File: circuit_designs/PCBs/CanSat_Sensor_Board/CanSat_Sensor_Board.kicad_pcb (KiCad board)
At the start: 4 copper layers, 100 x 100 mm, 32 parts

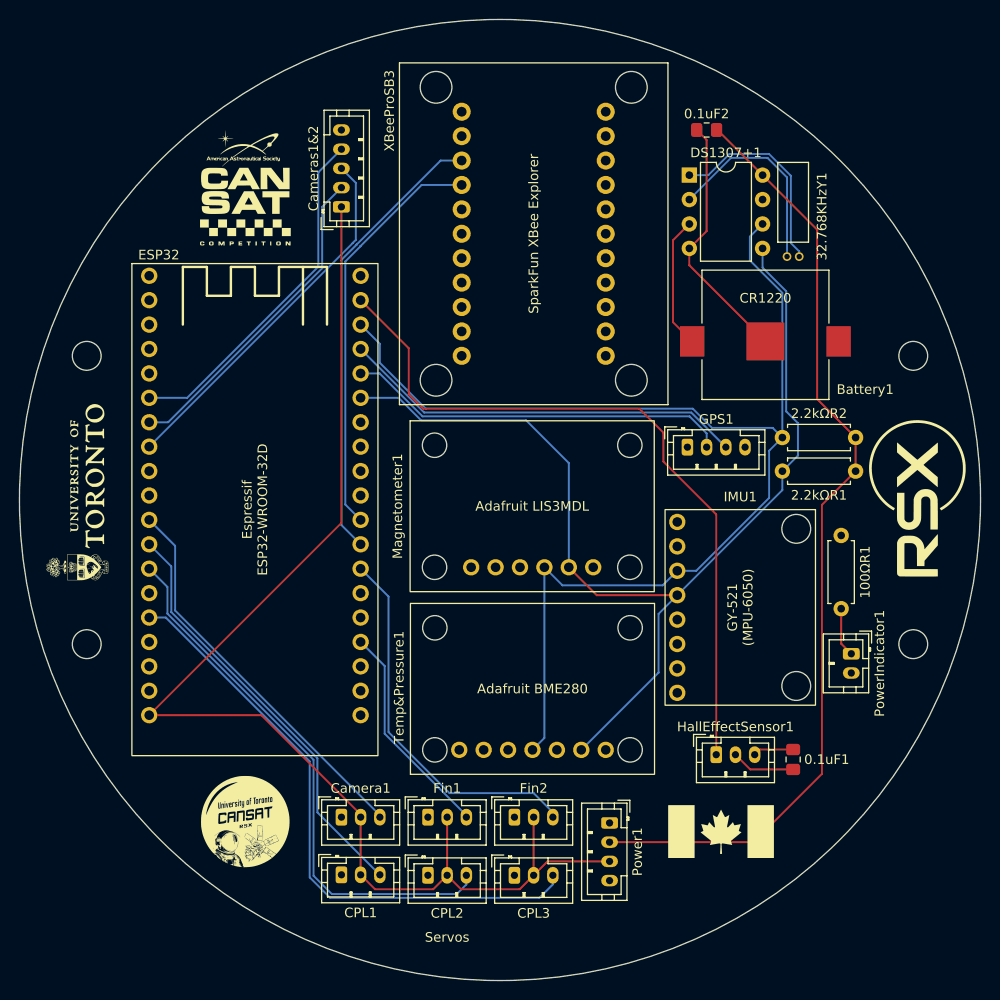
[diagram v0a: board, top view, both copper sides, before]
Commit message: Updating camera and sensor PCBs
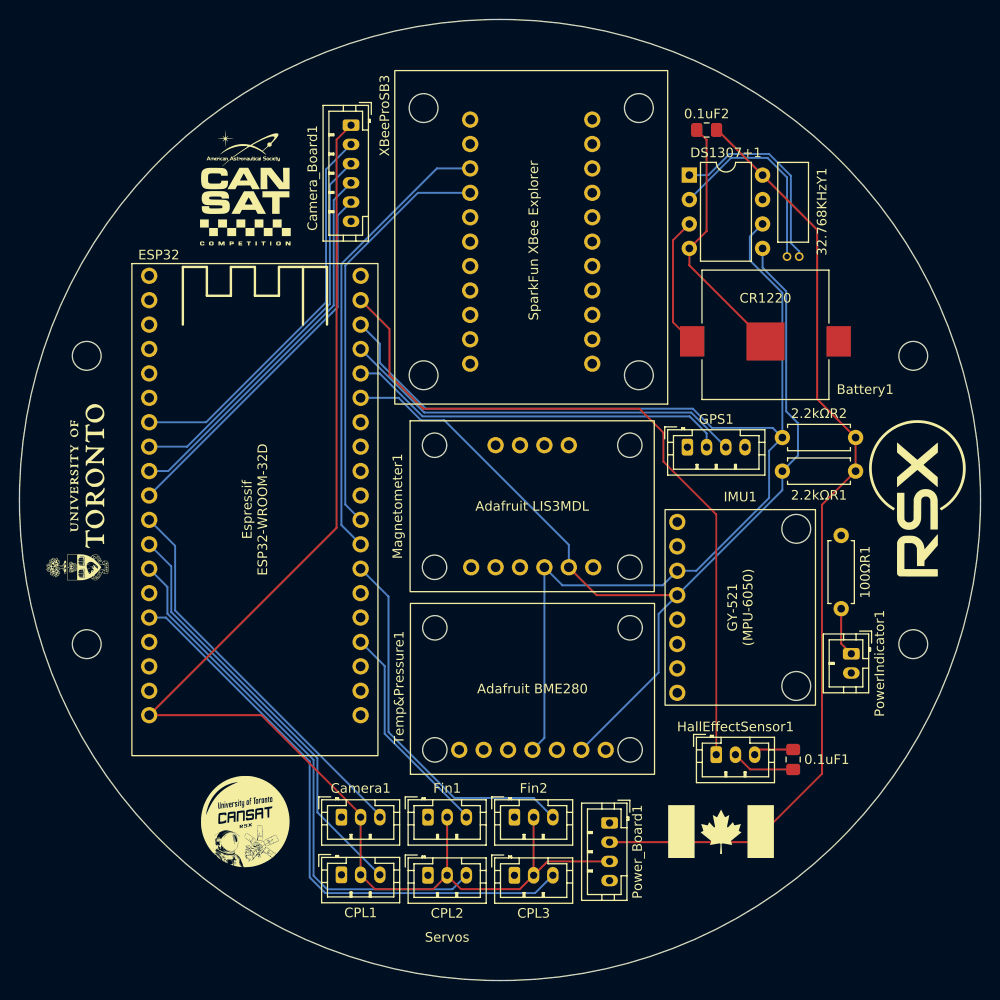
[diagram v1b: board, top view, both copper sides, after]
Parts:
- removed Cameras1&2: Conn_01x05_Pin, Connector_JST:JST_PH_B5B-PH-K_1x05_P2.00mm_Vertical
- added Camera_Board1: Conn_01x06_Pin, Connector_JST:JST_PH_B6B-PH-K_1x06_P2.00mm_Vertical, F.Cu at (134.5, 61.0)
- XBeeProSB3: footprint WRL-11812:MODULE_WRL-11812 -> Custom_Footprints:SparkFun_XBee_Explorer_Regulated
- moved XBeeProSB3 22.5 mm to (167.4, 90.0)
- renumbered Power1 to Power_Board1
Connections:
- ESP32 pad J2-10: unconnected-(ESP32-IO26-PadJ2-10) -> Net-(Camera_Board1-Pin_5)
- ESP32 pad J2-6: Net-(Cameras1&2-Pin_4) -> unconnected-(ESP32-IO35-PadJ2-6)
- ESP32 pad J2-9: unconnected-(ESP32-IO25-PadJ2-9) -> Net-(Camera_Board1-Pin_4)
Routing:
- net Net-(Camera_Board1-Pin_4): track 0.00 -> 39.8 mm
- net Net-(Camera_Board1-Pin_5): track 0.00 -> 39.2 mm
- net Net-(Cameras1&2-Pin_4): track 36.5 -> 0.00 mm
- net +7.4V: track 134.6 -> 143.5 mm
- net Net-(Camera_Board1-Pin_2): track 34.4 -> 41.1 mm
- net Net-(DS1307+1-SDA): track 111.1 -> 106.1 mm
- net Net-(Camera_Board1-Pin_3): track 38.5 -> 40.5 mm
- net Net-(CPL3-Pin_3): track 62.7 -> 61.7 mm
- net Net-(CPL2-Pin_3): track 57.1 -> 56.1 mm
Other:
- board text added: "Data1"
- board text added: "Data2"
- board text added: "Signal1"
- board text added: "Signal2"
- board text removed: "Cam1"
- board text removed: "Cam2"

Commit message: Updating new KiCad files
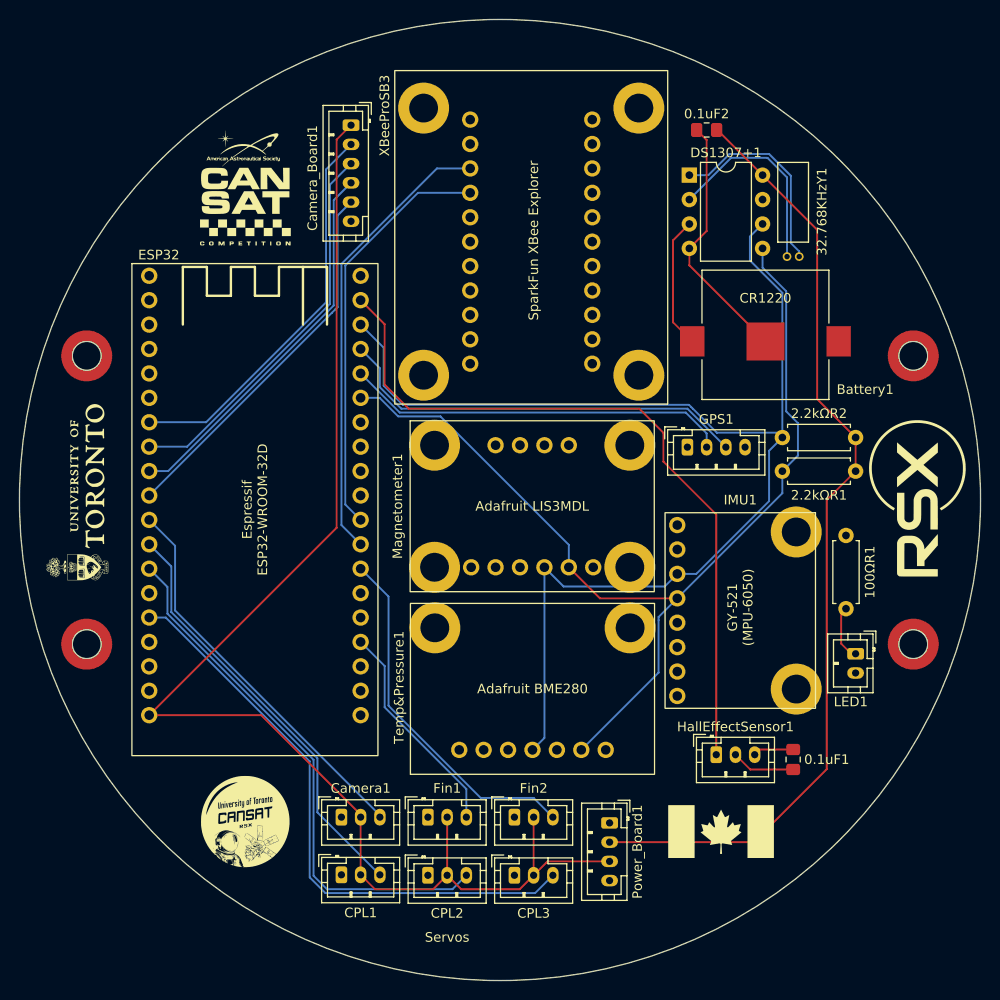
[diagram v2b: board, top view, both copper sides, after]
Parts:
- added REF**: WA-SMSI_9774030243, DigiKey:WA-SMSI_9774030243, F.Cu at (107.0, 85.0)
- added REF**: WA-SMSI_9774030243, DigiKey:WA-SMSI_9774030243, F.Cu at (193.0, 85.0)
- added REF**: WA-SMSI_9774030243, DigiKey:WA-SMSI_9774030243, F.Cu at (107.0, 115.0)
- added REF**: WA-SMSI_9774030243, DigiKey:WA-SMSI_9774030243, F.Cu at (193.0, 115.0)
- moved 100ΩR1 0.50 mm to (186.0, 111.3)
- moved LED1 0.45 mm to (187.0, 116.0)
- moved IMU1 0.33 mm to (182.8, 101.3)
- renumbered PowerIndicator1 to LED1
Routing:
- net Net-(ESP32-IO4): track 39.0 -> 37.4 mm
- net Net-(DS1307+1-SCL): track 128.9 -> 130.4 mm
- net Net-(ESP32-TXD0): track 42.2 -> 43.4 mm
- net Net-(ESP32-IO23): track 75.8 -> 76.7 mm
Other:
- outline, holes or cut-outs redrawn

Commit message: Final review submission of all CanSat PCB boards and corresponding custom KiCad 3D models, footprints, and symbols
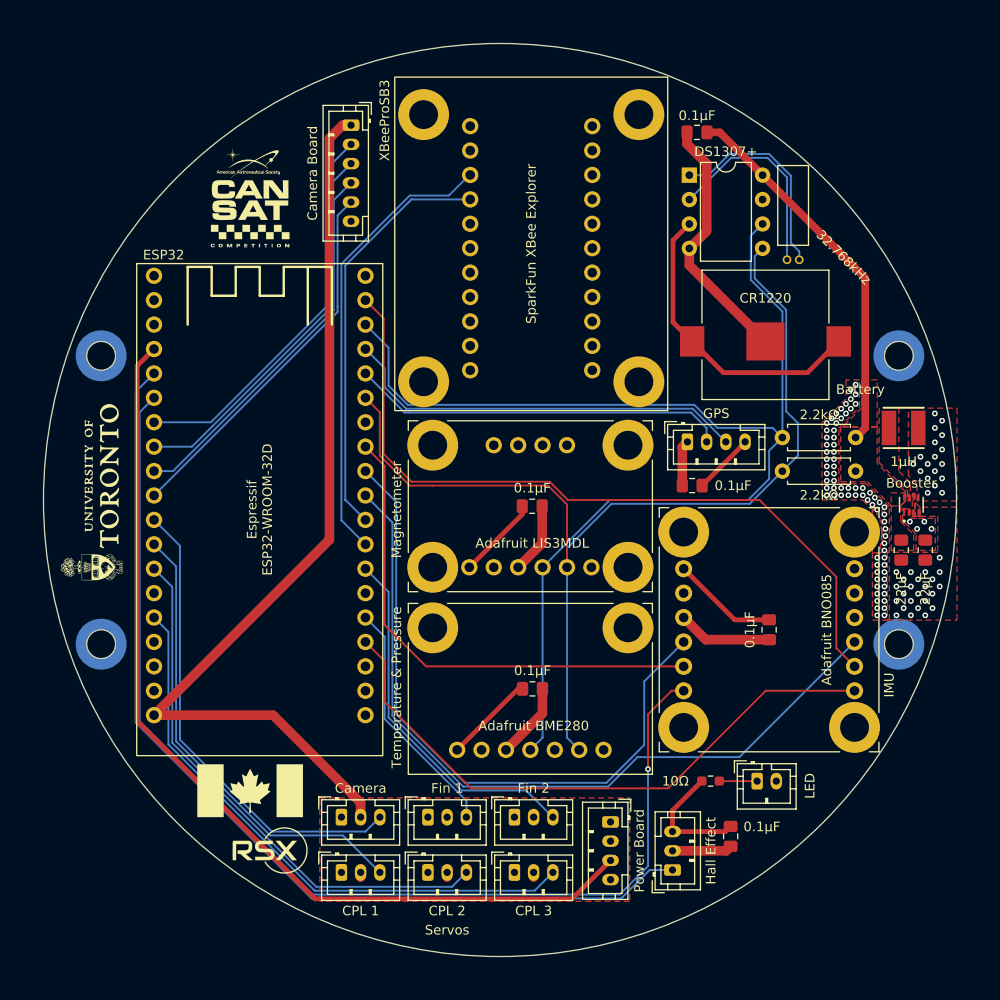
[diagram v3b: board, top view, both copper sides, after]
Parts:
- removed the G*** at (123.5, 67.5)
- removed the G*** at (193.5, 100.0)
- removed IMU1: GY-521_(MPU-6050), Custom_Footprints:GY-521_(MPU-6050)
- added Adafruit_BNO085_U5: IMU, Custom_Footprints:Adafruit_BNO085, F.Cu at (189.4, 100.8)
- added C2: 0.1μF, Capacitor_SMD:C_0805_2012Metric_Pad1.18x1.45mm_HandSolder, F.Cu at (153.4, 119.7)
- added C3: 0.1μF, Capacitor_SMD:C_0805_2012Metric_Pad1.18x1.45mm_HandSolder, F.Cu at (170.0, 98.5)
- added C4: 0.1μF, Capacitor_SMD:C_0805_2012Metric_Pad1.18x1.45mm_HandSolder, F.Cu at (153.3, 100.7)
- added C5: 0.1μF, Capacitor_SMD:C_0805_2012Metric_Pad1.18x1.45mm_HandSolder, F.Cu at (178.0, 113.5)
- added C7: 22μF, Capacitor_SMD:C_0805_2012Metric_Pad1.18x1.45mm_HandSolder, F.Cu at (194.2, 105.2)
- added C8: 22μF, Capacitor_SMD:C_0805_2012Metric_Pad1.18x1.45mm_HandSolder, F.Cu at (191.8, 105.2)
- added G***: LOGO, Graphics:cansat_logo_2, F.Cu at (124.0, 68.5)
- added G***: LOGO, Graphics:rsx_logo_3, F.Cu at (126.0, 136.5)
- added G***: LOGO, Graphics:rsx_logo_2, B.Cu at (153.0, 115.0)
- added TPS610333DRLR_U8: Booster, DigiKey:SOT-5X3-8_DRL_TEX, F.Cu at (192.8, 100.5)
- added WE-LQS_4025_L1: 1μH, DigiKey:WE-LQS_4025, F.Cu at (192.0, 92.5)
- 2894TR_U7: renamed from Battery1; value 2894TR -> Battery
- Adafruit_BME280_STEMMA_QT_U3: renamed from Temp&Pressure1; value Adafruit_BME280_STEMMA_QT -> Temperature & Pressure
- Adafruit_LIS3MDL_U4: renamed from Magnetometer1; value Adafruit_LIS3MDL -> Magnetometer
- C1: renamed from 0.1uF1; value C1 -> 0.1μF
- C6: renamed from 0.1uF2; value C2 -> 0.1μF
- ESP32-DEVKIT-32_U1: renamed from ESP32; value ESP32-DEVKITC-32D -> ESP32
- G***, REF** (x4): moved to B.Cu
- J1: renamed from Power_Board1; value Conn_01x04_Pin -> Power Board
- J10: renamed from CPL2; value Conn_01x03_Pin -> CPL 2
- J11: renamed from CPL3; value Conn_01x03_Pin -> CPL 3
- J2: renamed from Camera_Board1; value Conn_01x06_Pin -> Camera Board
- J3: renamed from HallEffectSensor1; value Conn_01x03_Pin -> Hall Effect
- J4: renamed from GPS1; value Conn_01x04_Pin -> GPS
- J5: renamed from LED1; value Conn_01x02_Pin -> LED
- J6: renamed from Fin1; value Conn_01x03_Pin -> Fin 1
- J7: renamed from Fin2; value Conn_01x03_Pin -> Fin 2
- J8: renamed from Camera1; value Conn_01x03_Pin -> Camera
- J9: renamed from CPL1; value Conn_01x03_Pin -> CPL 1
- R1: renamed from 100ΩR1; value R1 -> 10Ω; footprint Resistor_THT:R_Axial_DIN0207_L6.3mm_D2.5mm_P7.62mm_Horizontal -> Resistor_SMD:R_0603_1608Metric_Pad0.98x0.95mm_HandSolder
- R2: renamed from 2.2kΩR1; value R2 -> 2.2kΩ
- R3: renamed from 2.2kΩR2; value R3 -> 2.2kΩ
- SparkFunXBeeExplorer_U2: renamed from XBeeProSB3; value SparkFunXBeeExplorer1 -> XBeeProSB3
- Y1: renamed from 32.768KHzY1; value AB38T-32.768KHZ -> 32.768kHz
- moved G*** 62.0 mm to (178.0, 104.0), turned to 180 degrees
- moved G*** 49.2 mm to (124.0, 130.2)
- moved R1 22.8 mm to (171.9, 129.2), turned to 180 degrees
- moved J5 16.8 mm to (176.8, 129.2), turned to 0 degrees
- moved J3 12.8 mm to (167.9, 138.5), turned to 90 degrees
- moved C1 10.3 mm to (174.0, 135.0), turned to 90 degrees
- moved G*** 1.50 mm to (108.5, 97.5)
- moved G*** 1.50 mm to (107.5, 107.0)
- moved REF** 1.50 mm to (108.5, 85.0), turned to 180 degrees
- moved REF** 1.50 mm to (191.5, 85.0), turned to 180 degrees
- moved REF** 1.50 mm to (108.5, 115.0), turned to 180 degrees
- moved REF** 1.50 mm to (191.5, 115.0), turned to 180 degrees
- moved C6 1.03 mm to (170.5, 61.8)
- moved SparkFunXBeeExplorer_U2 0.68 mm to (167.4, 90.7)
- moved J4 0.55 mm to (169.5, 94.0)
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- renumbered DS1307+1 to DS1307+_U6
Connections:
- 2894TR_U7 pad P1: unconnected-(Battery1-PadP1) -> Net-(DS1307+_U6-VBAT)
- 2894TR_U7 pad P2: Net-(DS1307+1-VBAT) -> Net-(DS1307+_U6-VBAT)
- Adafruit_BME280_STEMMA_QT_U3 pad 1: +3.3V -> /3.3V
- Adafruit_LIS3MDL_U4 pad 1: +3.3V -> /3.3V
- C1 pad 1: +3.3V -> GND
- C1 pad 2: GND -> /3.3V
- C6 pad 2: +5V -> /5V
- DS1307+_U6 pad 3: Net-(DS1307+1-VBAT) -> Net-(DS1307+_U6-VBAT)
- DS1307+_U6 pad 8: +5V -> /5V
- ESP32-DEVKIT-32_U1 pad J2-19: +7.4V -> /7.4V
- ESP32-DEVKIT-32_U1 pad J2-4: unconnected-(ESP32-SENSOR_VN-PadJ2-4) -> /ADC
- ESP32-DEVKIT-32_U1 pad J2-5: unconnected-(ESP32-IO34-PadJ2-5) -> Net-(ESP32-DEVKIT-32_U1-IO34)
- ESP32-DEVKIT-32_U1 pad J2-6: unconnected-(ESP32-IO35-PadJ2-6) -> Net-(Adafruit_BNO085_U5-~{INT})
- ESP32-DEVKIT-32_U1 pad J3-10: unconnected-(ESP32-IO5-PadJ3-10) -> Net-(Adafruit_BNO085_U5-~{RST})
- ESP32-DEVKIT-32_U1 pad J3-15: unconnected-(ESP32-IO2-PadJ3-15) -> Net-(ESP32-DEVKIT-32_U1-IO2)
- ESP32-DEVKIT-32_U1 pad J3-16: Net-(ESP32-IO15) -> Net-(Adafruit_BNO085_U5-CS)
- ESP32-DEVKIT-32_U1 pad J3-2: Net-(ESP32-IO23) -> Net-(Adafruit_BNO085_U5-DI)
- ESP32-DEVKIT-32_U1 pad J3-8: unconnected-(ESP32-IO19-PadJ3-8) -> Net-(Adafruit_BNO085_U5-SDA)
- ESP32-DEVKIT-32_U1 pad J3-9: unconnected-(ESP32-IO18-PadJ3-9) -> Net-(Adafruit_BNO085_U5-SCL)
- J1 pad 1: +3.3V -> /3.3V
- J1 pad 2: +5V -> /7.4V
- J1 pad 3: +7.4V -> /ADC
- J10 pad 2: +7.4V -> /7.4V
- J11 pad 2: +7.4V -> /7.4V
- J2 pad 1: +7.4V -> /7.4V
- J3 pad 1: Net-(ESP32-IO23) -> Net-(ESP32-DEVKIT-32_U1-IO34)
- J3 pad 3: +3.3V -> /3.3V
- J4 pad 4: +3.3V -> /3.3V
- J6 pad 2: +7.4V -> /7.4V
- J6 pad 3: Net-(ESP32-IO15) -> Net-(ESP32-DEVKIT-32_U1-IO2)
- J7 pad 2: +7.4V -> /7.4V
- J8 pad 2: +7.4V -> /7.4V
- J9 pad 2: +7.4V -> /7.4V
- R1 pad 2: +3.3V -> /3.3V
- R2 pad 1: +5V -> /5V
- R3 pad 1: +5V -> /5V
- SparkFunXBeeExplorer_U2 pad JP5_10: +3.3V -> /3.3V
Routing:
- net +7.4V: track 143.5 -> 0.00 mm
- net Net-(Adafruit_BNO085_U5-~{INT}): track 0.00 -> 116.4 mm, vias 0 -> 1
- net Net-(ESP32-DEVKIT-32_U1-IO34): track 0.00 -> 101.8 mm
- net +5V: track 99.6 -> 0.00 mm
- net /7.4V: track 0.00 -> 98.8 mm
- net /ADC: track 0.00 -> 98.0 mm
- net Net-(Adafruit_BNO085_U5-~{RST}): track 0.00 -> 81.5 mm
- net Net-(Adafruit_BNO085_U5-DI): track 0.00 -> 79.3 mm
- net Net-(ESP32-IO23): track 76.7 -> 0.00 mm
- net Net-(Adafruit_BNO085_U5-SCL): track 0.00 -> 69.4 mm
- net Net-(Adafruit_BNO085_U5-CS): track 0.00 -> 63.9 mm
- net Net-(Adafruit_BNO085_U5-SDA): track 0.00 -> 52.3 mm
- net /3.3V: track 0.00 -> 48.7 mm, vias 0 -> 22
- net /5V: track 0.00 -> 40.0 mm
- net Net-(DS1307+_U6-VBAT): track 0.00 -> 31.7 mm
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- added copper zone on F.Cu, net /3.3V
- added copper zone on In2.Cu, net /3.3V
- added copper zone on F.Cu, net /5V
- added copper zone on F.Cu, net /7.4V
- added copper zone on F.Cu, net /SW
- added copper zone on F.Cu, net GND
- added copper zone on In1.Cu, net GND
- removed copper zone on In1.Cu, net +3.3V
- removed copper zone on In2.Cu, net GND
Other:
- board size 100 x 100 mm -> 95 x 95 mm
- board text added: "32.768kHz"
- board text added: "ADC"
- board text added: "Adafruit BNO085"
- board text added: "BT"
- board text added: "DI"
- board text added: "P0"
- board text added: "P1"
- board text removed: "100Ω"
- board text removed: "32.768KHz"
- board text removed: "ADO"
- board text removed: "GY-521 (MPU-6050)"
- board text removed: "XCL"
- board text removed: "XDA"

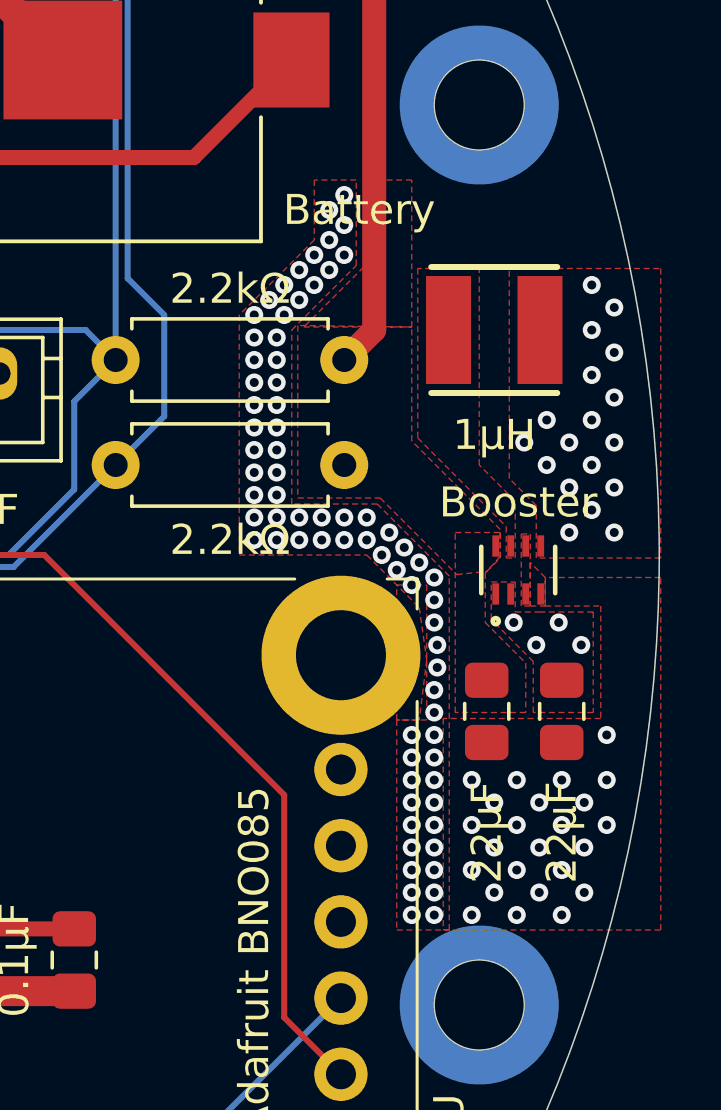
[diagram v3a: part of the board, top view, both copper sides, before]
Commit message: fixed stiching vias - added new logo - fixed some other vias with kc
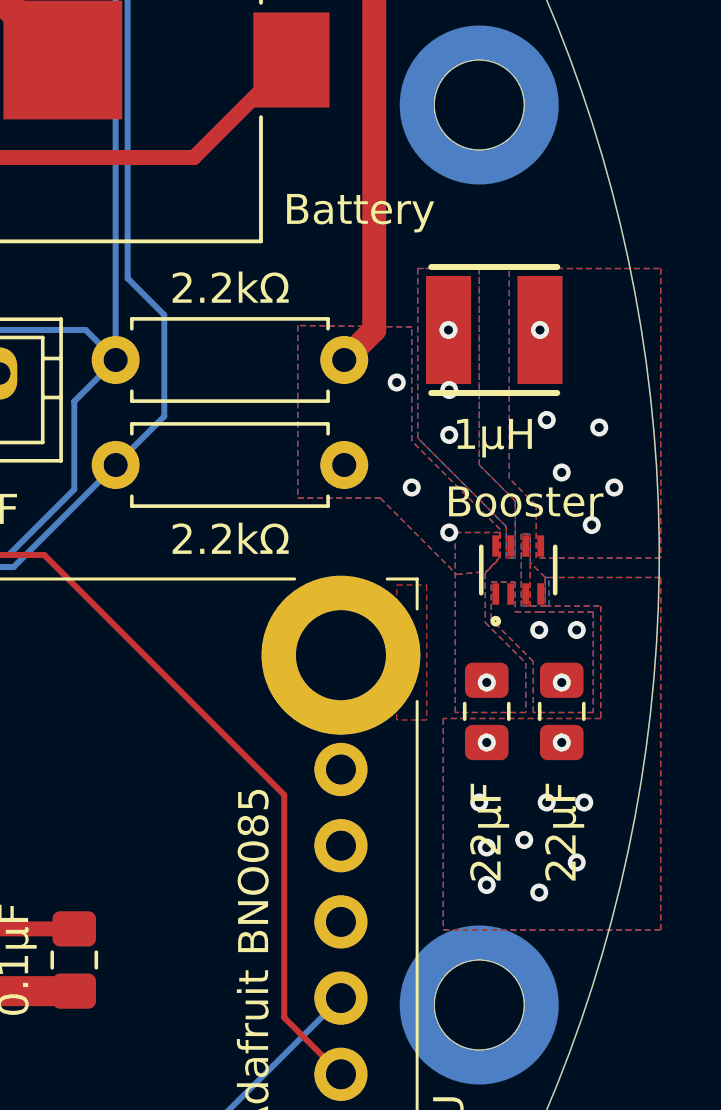
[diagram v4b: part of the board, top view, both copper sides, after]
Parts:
- added G***: LOGO, Graphics:logo, B.Cu at (178.2, 120.8)
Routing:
- net GND: vias 97 -> 10
- net /SW: vias 0 -> 3
- net /5V: vias 0 -> 4
- net /3.3V: vias 22 -> 9
- added copper zone on B.Cu, net /3.3V
- added copper zone on B.Cu, net /5V
- added copper zone on B.Cu, net /SW
- added copper zone on B.Cu, net GND
